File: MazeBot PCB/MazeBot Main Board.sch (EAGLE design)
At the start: 5 parts, among them IC1 7805TV

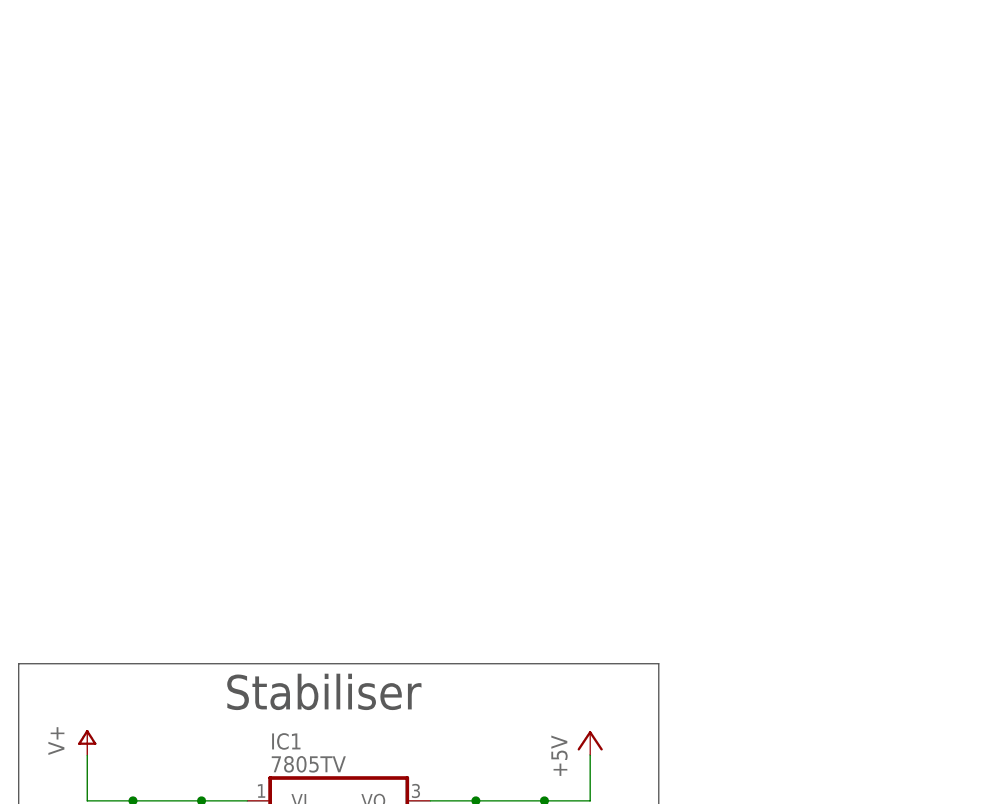
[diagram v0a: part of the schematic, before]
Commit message: Add ECU schematic
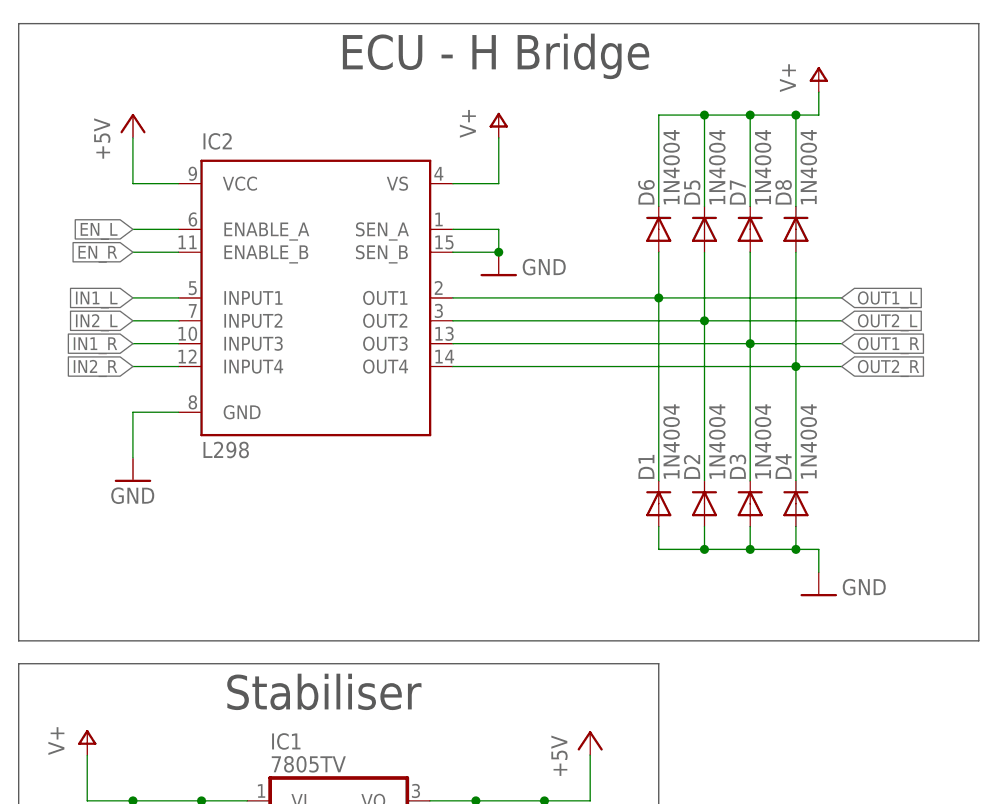
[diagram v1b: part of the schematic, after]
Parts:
- added D1, D2, D3, D4, D5, D6, D7, D8: 1N4004, diode:1N4004
- added IC2: L298, st-microelectronics:L298
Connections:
- new net EN_L: IC2.ENABLE_A
- new net EN_R: IC2.ENABLE_B
- new net IN1_L: IC2.INPUT1
- new net IN1_R: IC2.INPUT3
- new net IN2_L: IC2.INPUT2
- new net IN2_R: IC2.INPUT4
- new net OUT1_L: D1.C, D6.A, IC2.OUT1
- new net OUT1_R: D3.C, D7.A, IC2.OUT3
- new net OUT2_L: D2.C, D5.A, IC2.OUT2
- new net OUT2_R: D4.C, D8.A, IC2.OUT4
- net +5V: now also IC2.VCC
- net GND: now also D1.A, D2.A, D3.A, D4.A, IC2.GND, IC2.SEN_A, IC2.SEN_B
- net V+: now also D5.C, D6.C, D7.C, D8.C, IC2.VS
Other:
- note added: "ECU - H Bridge"

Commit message: Add ATMEGA with XTAL
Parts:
- added C1, C2: 100nF, rcl:C-EU025-024X044
- added Q1: (no value), special:XTAL/S
- added U$1: ATMEGA32U4-AU, adafruit:ATMEGA32U4-AU
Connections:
- new net N$1: C1.1, Q1.1, U$1.XTAL1
- new net N$2: C2.1, Q1.2, U$1.XTAL2
- net GND: now also C1.2, C2.2

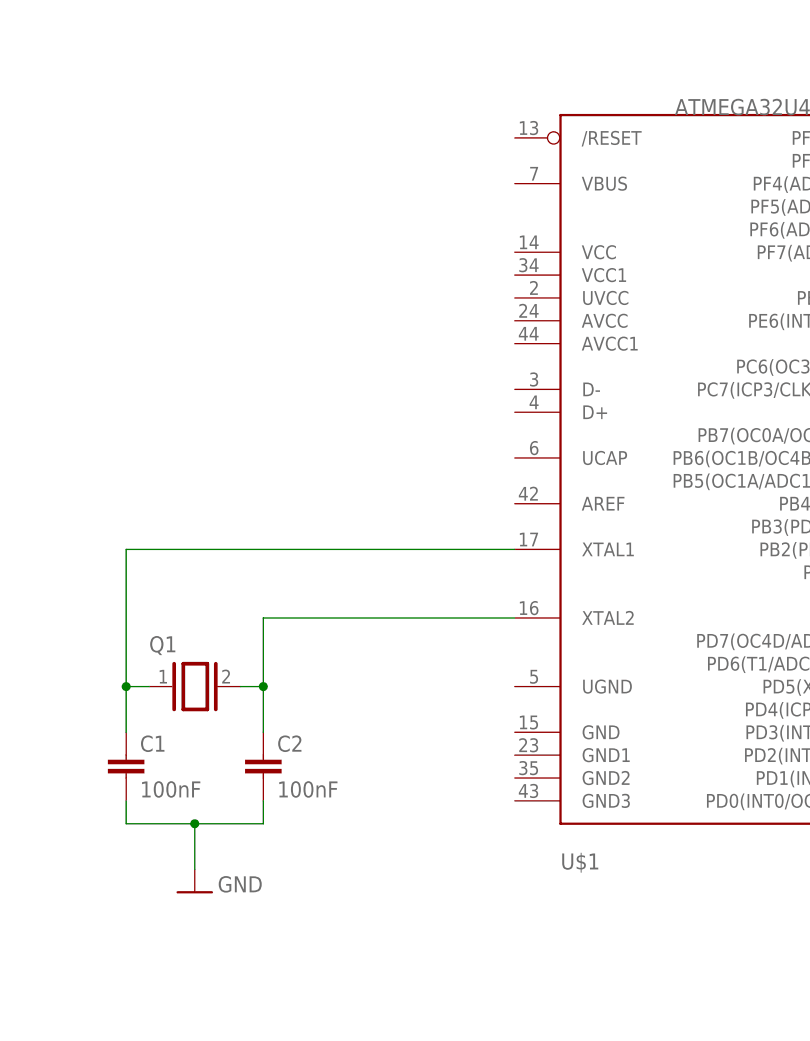
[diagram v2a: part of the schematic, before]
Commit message: Add power for ATMEGA
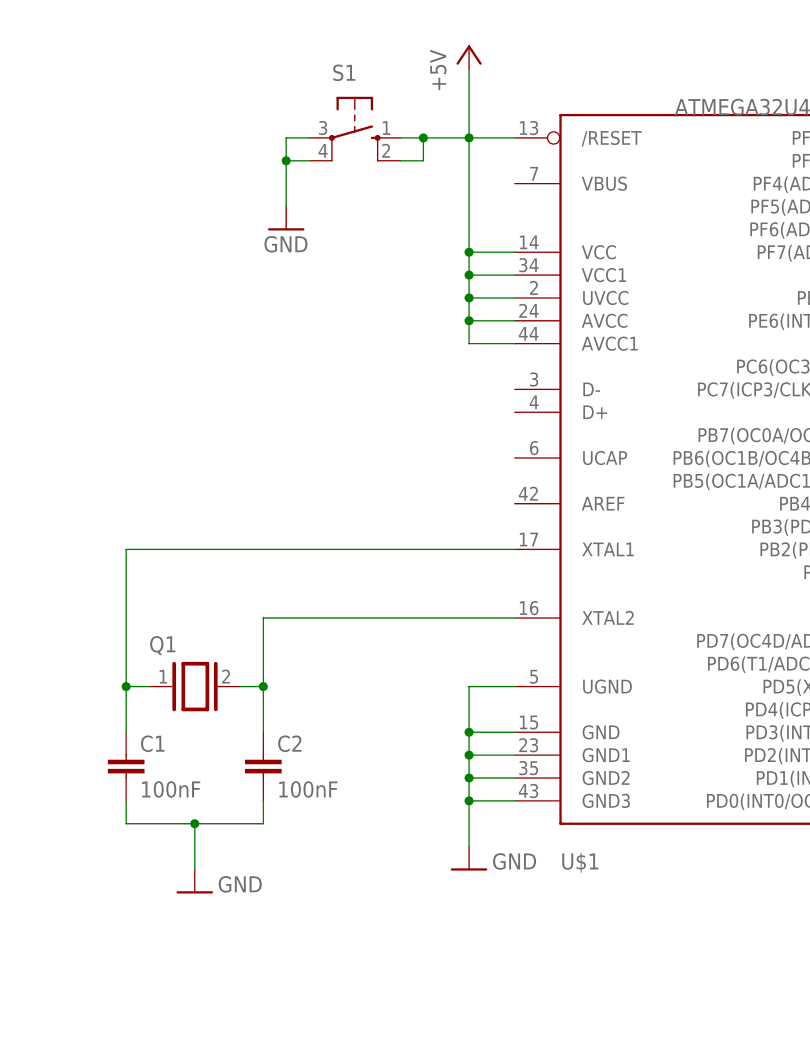
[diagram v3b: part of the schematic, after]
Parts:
- added S1: (no value), switch-omron:10-XX
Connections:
- net +5V: now also S1.S, S1.S1, U$1./RESET, U$1.AVCC, U$1.AVCC1, U$1.UVCC, U$1.VCC, U$1.VCC1
- net GND: now also S1.P, S1.P1, U$1.GND, U$1.GND1, U$1.GND2, U$1.GND3, U$1.UGND
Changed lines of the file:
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@@
 <part name="C2" library="rcl" library_urn="urn:adsk.eagle:library:334" deviceset="C-EU" device="025-024X044" package3d_urn="urn:adsk.eagle:package:23630/1" value="100nF"/>
 <part name="GND9" library="supply1" library_urn="urn:adsk.eagle:library:371" deviceset="GND" device=""/>
+<part name="P+6" library="supply1" library_urn="urn:adsk.eagle:library:371" deviceset="+5V" device=""/>
+<part name="GND10" library="supply1" library_urn="urn:adsk.eagle:library:371" deviceset="GND" device=""/>
+<part name="S1" library="switch-omron" library_urn="urn:adsk.eagle:library:377" deviceset="10-XX" device="" package3d_urn="urn:adsk.eagle:package:27496/1"/>
+<part name="GND11" library="supply1" library_urn="urn:adsk.eagle:library:371" deviceset="GND" device=""/>
 </parts>
 <sheets>
@@
 <attribute name="VALUE" x="154.94" y="20.32" size="1.778" layer="96"/>
 </instance>
+<instance part="P+6" gate="1" x="182.88" y="114.3" smashed="yes">
+<attribute name="VALUE" x="180.34" y="109.22" size="1.778" layer="96" rot="R90"/>
+</instance>
+<instance part="GND10" gate="1" x="182.88" y="22.86" smashed="yes">
+<attribute name="VALUE" x="185.42" y="22.86" size="1.778" layer="96"/>
+</instance>
+<instance part="S1" gate="1" x="170.18" y="104.14" smashed="yes" rot="R270">
+<attribute name="NAME" x="167.64" y="110.49" size="1.778" layer="95"/>
+<attribute name="VALUE" x="173.355" y="107.95" size="1.778" layer="96"/>
+</instance>
+<instance part="GND11" gate="1" x="162.56" y="93.98" smashed="yes">
+<attribute name="VALUE" x="160.02" y="91.44" size="1.778" layer="96"/>
+</instance>
 </instances>
 <busses>
@@
 <wire x1="17.78" y1="99.06" x2="22.86" y2="99.06" width="0.1524" layer="91"/>
 </segment>
+<segment>
+<pinref part="U$1" gate="G$1" pin="VCC"/>
+<wire x1="187.96" y1="91.44" x2="182.88" y2="91.44" width="0.1524" layer="91"/>
+<pinref part="U$1" gate="G$1" pin="AVCC1"/>
+<wire x1="187.96" y1="81.28" x2="182.88" y2="81.28" width="0.1524" layer="91"/>
+<wire x1="182.88" y1="91.44" x2="182.88" y2="88.9" width="0.1524" layer="91"/>
+<junction x="182.88" y="91.44"/>
+<wire x1="182.88" y1="88.9" x2="182.88" y2="86.36" width="0.1524" layer="91"/>
+<wire x1="182.88" y1="86.36" x2="182.88" y2="83.82" width="0.1524" layer="91"/>
+<wire x1="182.88" y1="83.82" x2="182.88" y2="81.28" width="0.1524" layer="91"/>
+<wire x1="182.88" y1="91.44" x2="182.88" y2="104.14" width="0.1524" layer="91"/>
+<pinref part="P+6" gate="1" pin="+5V"/>
+<pinref part="U$1" gate="G$1" pin="VCC1"/>
+<wire x1="182.88" y1="104.14" x2="182.88" y2="111.76" width="0.1524" layer="91"/>
+<wire x1="187.96" y1="88.9" x2="182.88" y2="88.9" width="0.1524" layer="91"/>
+<junction x="182.88" y="88.9"/>
+<pinref part="U$1" gate="G$1" pin="UVCC"/>
+<wire x1="187.96" y1="86.36" x2="182.88" y2="86.36" width="0.1524" layer="91"/>
+<junction x="182.88" y="86.36"/>
+<pinref part="U$1" gate="G$1" pin="AVCC"/>
+<wire x1="187.96" y1="83.82" x2="182.88" y2="83.82" width="0.1524" layer="91"/>
+<junction x="182.88" y="83.82"/>
+<pinref part="S1" gate="1" pin="S"/>
+<wire x1="175.26" y1="104.14" x2="177.8" y2="104.14" width="0.1524" layer="91"/>
+<pinref part="S1" gate="1" pin="S1"/>
+<wire x1="177.8" y1="104.14" x2="177.8" y2="101.6" width="0.1524" layer="91"/>
+<wire x1="177.8" y1="101.6" x2="175.26" y2="101.6" width="0.1524" layer="91"/>
+<pinref part="U$1" gate="G$1" pin="/RESET"/>
+<wire x1="177.8" y1="104.14" x2="182.88" y2="104.14" width="0.1524" layer="91"/>
+<junction x="177.8" y="104.14"/>
+<junction x="182.88" y="104.14"/>
+<wire x1="182.88" y1="104.14" x2="187.96" y2="104.14" width="0.1524" layer="91"/>
+</segment>
 </net>
 <net name="GND" class="0">
@@
 <junction x="152.4" y="27.94"/>
 </segment>
+<segment>
+<pinref part="U$1" gate="G$1" pin="UGND"/>
+<wire x1="187.96" y1="43.18" x2="182.88" y2="43.18" width="0.1524" layer="91"/>
+<wire x1="182.88" y1="43.18" x2="182.88" y2="38.1" width="0.1524" layer="91"/>
+<pinref part="U$1" gate="G$1" pin="GND"/>
+<wire x1="182.88" y1="38.1" x2="182.88" y2="35.56" width="0.1524" layer="91"/>
+<wire x1="182.88" y1="35.56" x2="182.88" y2="33.02" width="0.1524" layer="91"/>
+<wire x1="182.88" y1="33.02" x2="182.88" y2="30.48" width="0.1524" layer="91"/>
+<wire x1="182.88" y1="30.48" x2="182.88" y2="25.4" width="0.1524" layer="91"/>
+<wire x1="187.96" y1="38.1" x2="182.88" y2="38.1" width="0.1524" layer="91"/>
+<junction x="182.88" y="38.1"/>
+<pinref part="U$1" gate="G$1" pin="GND1"/>
+<wire x1="187.96" y1="35.56" x2="182.88" y2="35.56" width="0.1524" layer="91"/>
+<junction x="182.88" y="35.56"/>
+<pinref part="U$1" gate="G$1" pin="GND2"/>
+<wire x1="187.96" y1="33.02" x2="182.88" y2="33.02" width="0.1524" layer="91"/>
+<junction x="182.88" y="33.02"/>
+<pinref part="U$1" gate="G$1" pin="GND3"/>
+<wire x1="187.96" y1="30.48" x2="182.88" y2="30.48" width="0.1524" layer="91"/>
+<junction x="182.88" y="30.48"/>
+<pinref part="GND10" gate="1" pin="GND"/>
+</segment>
+<segment>
+<pinref part="S1" gate="1" pin="P1"/>
+<wire x1="165.1" y1="101.6" x2="162.56" y2="101.6" width="0.1524" layer="91"/>
+<wire x1="162.56" y1="101.6" x2="162.56" y2="104.14" width="0.1524" layer="91"/>
+<pinref part="S1" gate="1" pin="P"/>
+<wire x1="162.56" y1="104.14" x2="165.1" y2="104.14" width="0.1524" layer="91"/>
+<wire x1="162.56" y1="101.6" x2="162.56" y2="96.52" width="0.1524" layer="91"/>
+<junction x="162.56" y="101.6"/>
+<pinref part="GND11" gate="1" pin="GND"/>
+</segment>
 </net>

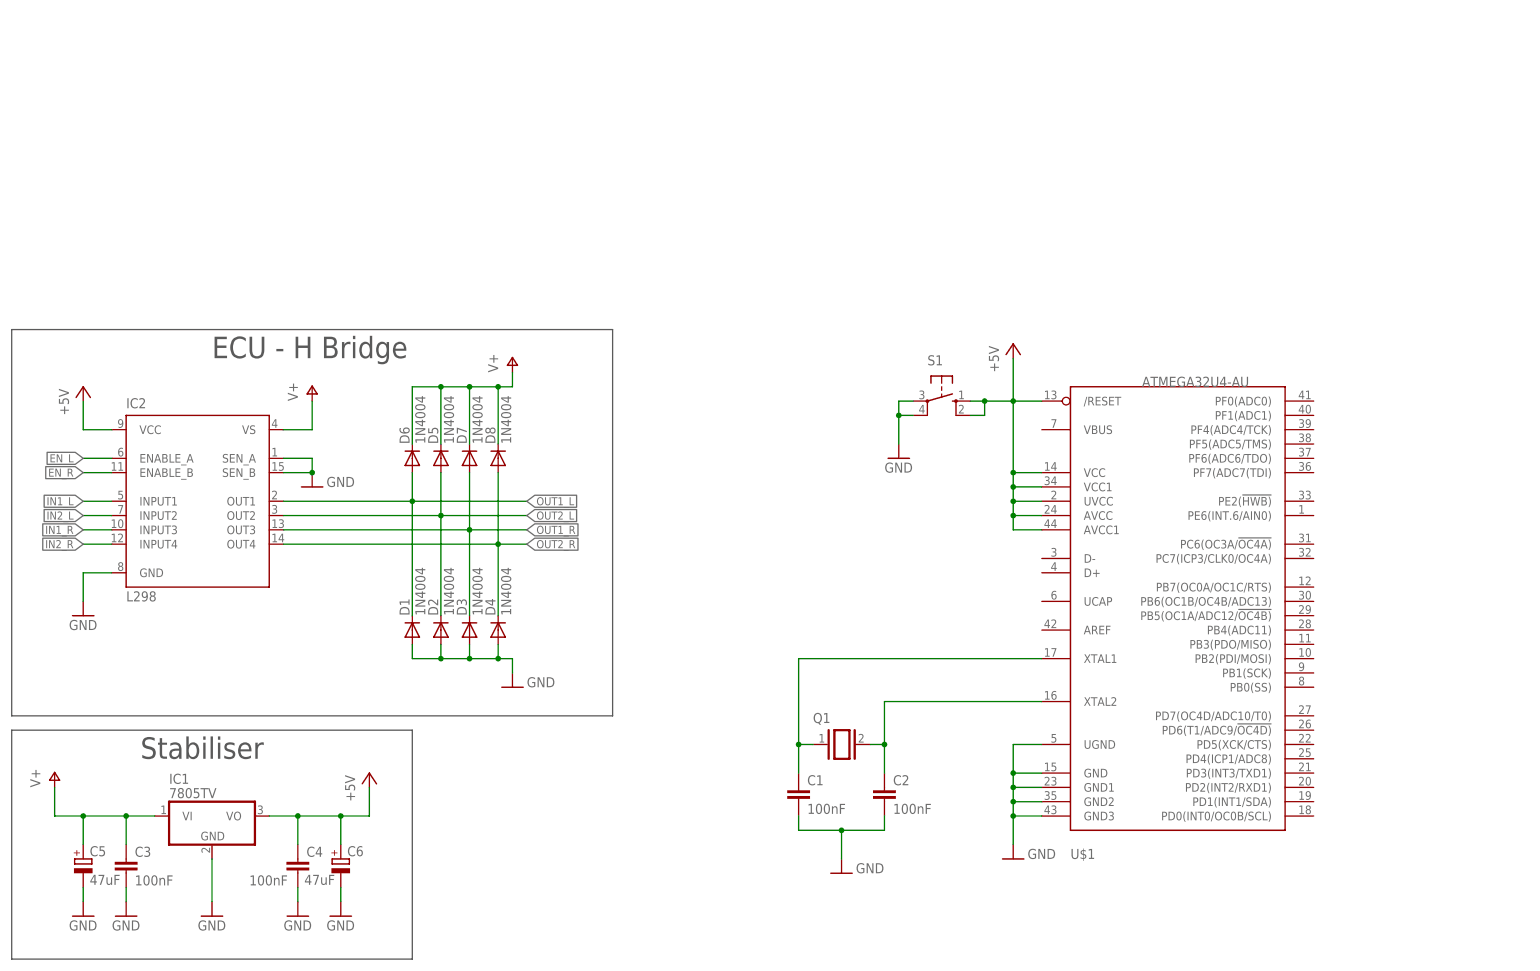
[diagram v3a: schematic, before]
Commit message: Wire ICSP for ATMEGA
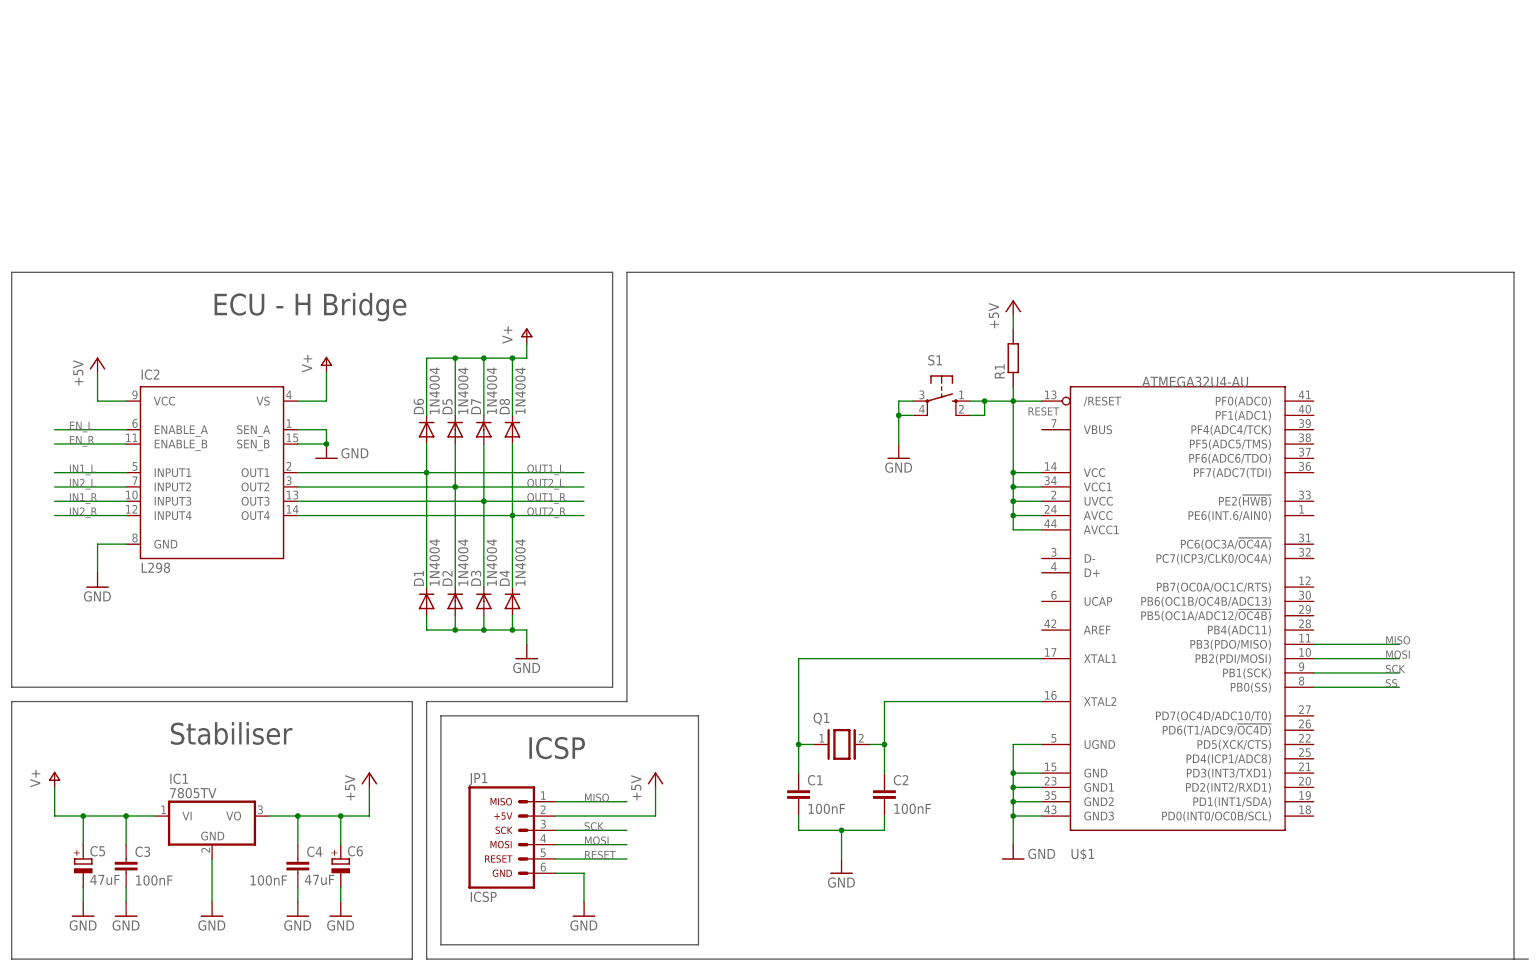
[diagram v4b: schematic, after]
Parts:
- added JP1: (no value), arduino_jw:ARDUINO_CONN-ICSP
- added R1: (no value), rcl:R-EU_0207/10
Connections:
- new net MISO: JP1.1, U$1.PB3(PDO/MISO)
- new net MOSI: JP1.4, U$1.PB2(PDI/MOSI)
- new net RESET: JP1.5, R1.1, S1.S, S1.S1, U$1./RESET, U$1.AVCC, U$1.AVCC1, U$1.UVCC, U$1.VCC, U$1.VCC1
- new net SCK: JP1.3, U$1.PB1(SCK)
- new net SS: U$1.PB0(SS)
- net +5V: now also JP1.2, R1.2; no longer S1.S, S1.S1, U$1./RESET, U$1.AVCC, U$1.AVCC1, U$1.UVCC, U$1.VCC, U$1.VCC1
- net GND: now also JP1.6
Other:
- note added: "ICSP"
- moved on the sheet: D1, D2, D3, D4, D5, D6, D7, D8, IC2
